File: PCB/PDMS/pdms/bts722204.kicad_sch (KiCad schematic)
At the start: 22 parts, among them IC7 BTS722204ESAXUMA1

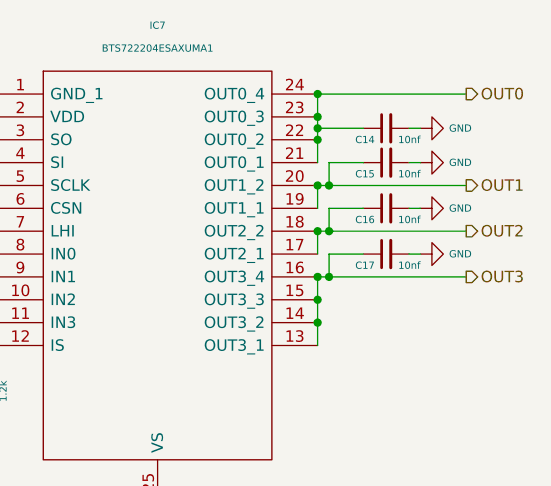
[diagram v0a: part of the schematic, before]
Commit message: Mostly assigned footprints
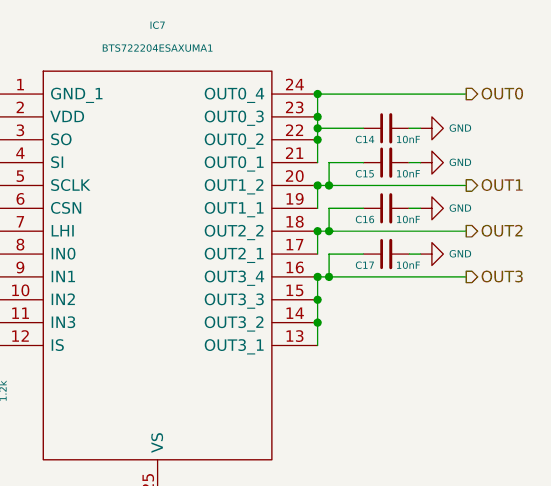
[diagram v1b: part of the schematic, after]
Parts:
- C14, C15, C16, C17: value 10nf -> 10nF
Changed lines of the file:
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@@
       (effects (font (size 0.8 0.8)) (justify left))
     )
-    (property "Value" "10nf" (id 1) (at 107.95 57.15 90)
+    (property "Value" "10nF" (id 1) (at 107.95 57.15 90)
       (effects (font (size 0.8 0.8)) (justify left))
     )
@@
       (effects (font (size 0.8 0.8)) (justify left))
     )
-    (property "Value" "10nf" (id 1) (at 107.95 48.26 90)
+    (property "Value" "10nF" (id 1) (at 107.95 48.26 90)
       (effects (font (size 0.8 0.8)) (justify left))
     )
@@
       (effects (font (size 0.8 0.8)) (justify left))
     )
-    (property "Value" "10nf" (id 1) (at 107.95 62.23 90)
+    (property "Value" "10nF" (id 1) (at 107.95 62.23 90)
       (effects (font (size 0.8 0.8)) (justify left))
     )
@@
       (effects (font (size 0.8 0.8)) (justify left))
     )
-    (property "Value" "10nf" (id 1) (at 107.95 52.07 90)
-      (effects (font (size 0.8 0.8)) (justify left))
-    )
+    (property "Value" "10nF" (id 1) (at 107.95 52.07 90)
+      (effects (font (size 0.8 0.8)) (justify left))
+    )

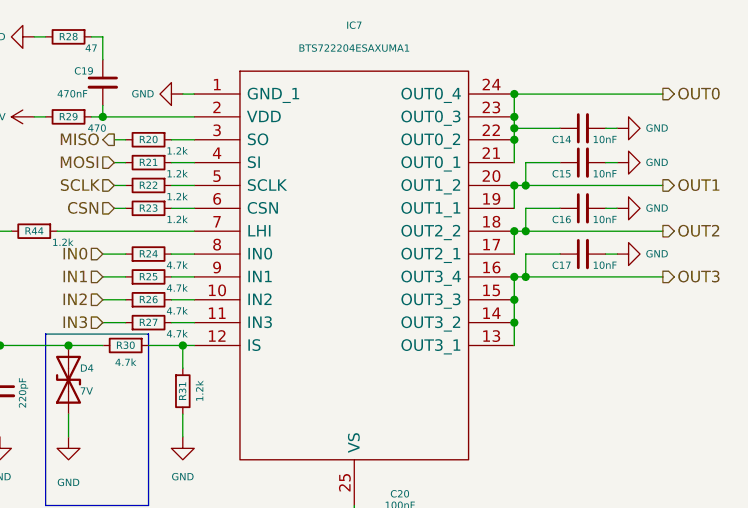
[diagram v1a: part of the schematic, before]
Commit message: Medium power stage layout
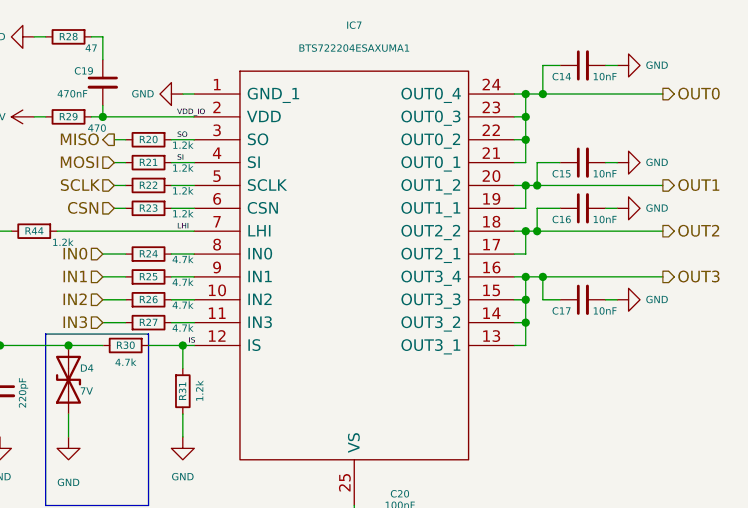
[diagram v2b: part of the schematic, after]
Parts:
- C14, C15, C16, C17: footprint Capacitor_SMD:C_0805_2012Metric -> Capacitor_SMD:C_0603_1608Metric
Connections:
- net LHI: now reaches IC7.7 (LHI), R44.1
- net VDD_IO: now reaches C19.2, IC7.2 (VDD), R29.1
- net IS: now reaches IC7.12 (IS), R30.1, R31.1
- net SO: now reaches IC7.3 (SO), R20.1
- net SI: now reaches IC7.4 (SI), R21.1
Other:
- moved on the sheet: C14, C17

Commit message: Imported 3.3V section with problematic shitty plugin
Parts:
- IC7: footprint PDM_Additional:SOP65P600X115-25N -> PDMS_Additional:SOP65P600X115-25N
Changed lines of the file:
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@@
       (effects (font (size 0.8 0.8)))
     )
-    (property "Footprint" "PDM_Additional:SOP65P600X115-25N" (id 2) (at 92.71 40.64 0)
+    (property "Footprint" "PDMS_Additional:SOP65P600X115-25N" (id 2) (at 92.71 40.64 0)
       (effects (font (size 1.27 1.27)) (justify left) hide)
     )

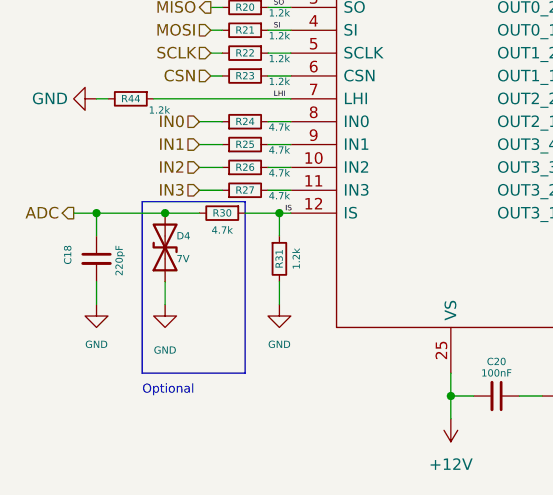
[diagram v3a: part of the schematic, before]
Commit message: Safety section - 74
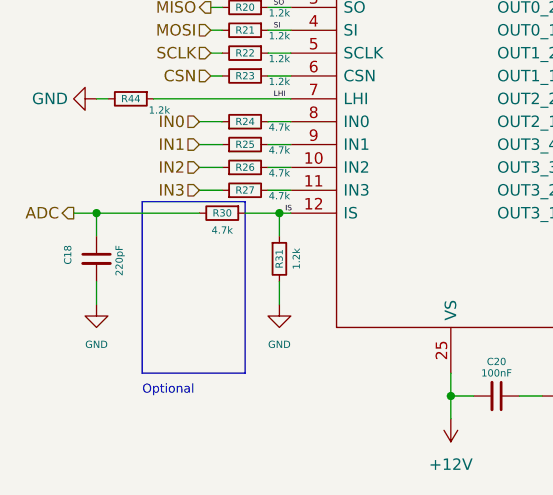
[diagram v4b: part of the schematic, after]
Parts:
- removed D4: 7V, Diode_SMD:D_0805_2012Metric, symbol Device:D_TVS
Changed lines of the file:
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@@
   (junction (at 97.79 58.42) (diameter 0) (color 0 0 0 0)
   )
-  (junction (at 46.99 71.12) (diameter 0) (color 0 0 0 0)
-  )
   (junction (at 97.79 68.58) (diameter 0) (color 0 0 0 0)
   )
@@
     (stroke (width 0) (type default) (color 0 0 0 0))
   )
-  (wire (pts (xy 39.37 71.12) (xy 46.99 71.12))
+  (wire (pts (xy 39.37 71.12) (xy 50.8 71.12))
     (stroke (width 0) (type default) (color 0 0 0 0))
   )
@@
     (stroke (width 0) (type default) (color 0 0 0 0))
   )
-  (wire (pts (xy 46.99 78.74) (xy 46.99 81.28))
-    (stroke (width 0) (type default) (color 0 0 0 0))
-  )
   (wire (pts (xy 58.42 53.34) (xy 60.96 53.34))
     (stroke (width 0) (type default) (color 0 0 0 0))
@@
   )
   (wire (pts (xy 101.6 55.88) (xy 99.06 55.88))
-    (stroke (width 0) (type default) (color 0 0 0 0))
-  )
-  (wire (pts (xy 46.99 71.12) (xy 50.8 71.12))
     (stroke (width 0) (type default) (color 0 0 0 0))
   )
@@
     (pin "9")
   )
-  (symbol (lib_id "power:GND") (at 46.99 81.28 0) (unit 1)
-    (in_bom yes) (on_board yes) (fields_autoplaced)
-    (property "Reference" "#PWR0134" (id 0) (at 46.99 87.63 0)
-      (effects (font (size 0.8 0.8)) hide)
-    )
-    (property "Value" "GND" (id 1) (at 46.99 86.36 0)
-      (effects (font (size 0.8 0.8)))
-    )
-    (property "Footprint" "" (id 2) (at 46.99 81.28 0)
-      (effects (font (size 1.27 1.27)) hide)
-    )
-    (property "Datasheet" "" (id 3) (at 46.99 81.28 0)
-      (effects (font (size 1.27 1.27)) hide)
-    )
-    (pin "1")
-  )
   (symbol (lib_id "power:GND") (at 107.95 66.04 90) (unit 1)
     (in_bom yes) (on_board yes) (fields_autoplaced)
@@
     (pin "1")
   )
-  (symbol (lib_id "Device:D_TVS") (at 46.99 74.93 90) (unit 1)
-    (in_bom yes) (on_board yes)
-    (property "Reference" "D4" (id 0) (at 48.26 73.66 90)
-      (effects (font (size 0.8 0.8)) (justify right))
-    )
-    (property "Value" "7V" (id 1) (at 48.26 76.2 90)
-      (effects (font (size 0.8 0.8)) (justify right))
-    )
-    (property "Footprint" "Diode_SMD:D_0805_2012Metric" (id 2) (at 46.99 74.93 0)
-      (effects (font (size 1.27 1.27)) hide)
-    )
-    (property "Datasheet" "~" (id 3) (at 46.99 74.93 0)
-      (effects (font (size 1.27 1.27)) hide)
-    )
-    (pin "1")
-    (pin "2")
-  )
   (symbol (lib_id "power:GND") (at 107.95 50.8 90) (unit 1)

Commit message: Major changes with new switch
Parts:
- added D39: BAT54SW, Package_TO_SOT_SMD:SOT-323_SC-70, symbol Diode:BAT54SW
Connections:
- net +3.3V: now also D39.2
- net ADC: now also D39.3
- net GND: now also D39.1
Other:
- note removed: "Optional"
- moved on the sheet: C18
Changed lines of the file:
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@@
   (junction (at 59.69 71.12) (diameter 0) (color 0 0 0 0)
   )
+  (junction (at 33.02 71.12) (diameter 0) (color 0 0 0 0)
+  )
   (junction (at 97.79 43.18) (diameter 0) (color 0 0 0 0)
   )
@@
   (junction (at 99.06 58.42) (diameter 0) (color 0 0 0 0)
   )
-  (junction (at 39.37 71.12) (diameter 0) (color 0 0 0 0)
+  (junction (at 45.974 71.12) (diameter 0) (color 0 0 0 0)
   )
   (junction (at 97.79 48.26) (diameter 0) (color 0 0 0 0)
@@
     (stroke (width 0) (type default) (color 0 0 0 0))
   )
-  (wire (pts (xy 39.37 71.12) (xy 50.8 71.12))
+  (wire (pts (xy 45.974 71.12) (xy 50.8 71.12))
     (stroke (width 0) (type default) (color 0 0 0 0))
   )
@@
     (stroke (width 0) (type default) (color 0 0 0 0))
   )
-  (polyline (pts (xy 44.45 69.85) (xy 44.45 88.9))
-    (stroke (width 0) (type default) (color 0 0 0 0))
-  )
   (wire (pts (xy 97.79 66.04) (xy 97.79 68.58))
     (stroke (width 0) (type default) (color 0 0 0 0))
@@
     (stroke (width 0) (type default) (color 0 0 0 0))
   )
-  (polyline (pts (xy 44.45 69.85) (xy 55.88 69.85))
-    (stroke (width 0) (type default) (color 0 0 0 0))
-  )
   (wire (pts (xy 50.8 66.04) (xy 53.34 66.04))
     (stroke (width 0) (type default) (color 0 0 0 0))
@@
     (stroke (width 0) (type default) (color 0 0 0 0))
   )
-  (wire (pts (xy 39.37 71.12) (xy 39.37 73.66))
+  (wire (pts (xy 45.974 71.12) (xy 45.974 73.66))
     (stroke (width 0) (type default) (color 0 0 0 0))
   )
@@
     (stroke (width 0) (type default) (color 0 0 0 0))
   )
+  (wire (pts (xy 41.275 80.772) (xy 40.64 80.772))
+    (stroke (width 0) (type default) (color 0 0 0 0))
+  )
   (wire (pts (xy 50.8 60.96) (xy 53.34 60.96))
     (stroke (width 0) (type default) (color 0 0 0 0))
@@
     (stroke (width 0) (type default) (color 0 0 0 0))
   )
-  (wire (pts (xy 36.83 71.12) (xy 39.37 71.12))
+  (wire (pts (xy 26.924 71.12) (xy 33.02 71.12))
     (stroke (width 0) (type default) (color 0 0 0 0))
   )
@@
     (stroke (width 0) (type default) (color 0 0 0 0))
   )
-  (wire (pts (xy 39.37 78.74) (xy 39.37 81.28))
+  (wire (pts (xy 45.974 78.74) (xy 45.974 80.772))
     (stroke (width 0) (type default) (color 0 0 0 0))
   )
@@
     (stroke (width 0) (type default) (color 0 0 0 0))
   )
-  (polyline (pts (xy 44.45 88.9) (xy 55.88 88.9))
-    (stroke (width 0) (type default) (color 0 0 0 0))
-  )
   (wire (pts (xy 55.88 71.12) (xy 59.69 71.12))
     (stroke (width 0) (type default) (color 0 0 0 0))
@@
     (stroke (width 0) (type default) (color 0 0 0 0))
   )
-  (polyline (pts (xy 55.88 88.9) (xy 55.88 69.85))
-    (stroke (width 0) (type default) (color 0 0 0 0))
-  )
   (wire (pts (xy 97.79 71.12) (xy 96.52 71.12))
     (stroke (width 0) (type default) (color 0 0 0 0))
   )
+  (wire (pts (xy 33.02 71.12) (xy 33.02 75.692))
+    (stroke (width 0) (type default) (color 0 0 0 0))
+  )
   (wire (pts (xy 97.79 48.26) (xy 97.79 45.72))
     (stroke (width 0) (type default) (color 0 0 0 0))
@@
     (stroke (width 0) (type default) (color 0 0 0 0))
   )
+  (wire (pts (xy 24.765 80.772) (xy 25.4 80.772))
+    (stroke (width 0) (type default) (color 0 0 0 0))
+  )
   (wire (pts (xy 59.69 78.74) (xy 59.69 81.28))
     (stroke (width 0) (type default) (color 0 0 0 0))
@@
     (stroke (width 0) (type default) (color 0 0 0 0))
   )
+  (wire (pts (xy 33.02 71.12) (xy 45.974 71.12))
+    (stroke (width 0) (type default) (color 0 0 0 0))
+  )
   (wire (pts (xy 78.74 91.44) (xy 81.28 91.44))
     (stroke (width 0) (type default) (color 0 0 0 0))
@@
   (wire (pts (xy 97.79 63.5) (xy 97.79 66.04))
     (stroke (width 0) (type default) (color 0 0 0 0))
-  )
-  (text "Optional" (at 44.45 91.44 0)
-    (effects (font (size 1 1)) (justify left bottom))
   )
   (label "IS" (at 60.325 71.12 0)
@@
     (effects (font (size 1.27 1.27)) (justify left))
   )
-  (hierarchical_label "ADC" (shape output) (at 36.83 71.12 180)
+  (hierarchical_label "ADC" (shape output) (at 26.924 71.12 180)
     (effects (font (size 1.27 1.27)) (justify right))
   )
   (hierarchical_label "IN3" (shape input) (at 50.8 68.58 180)
     (effects (font (size 1.27 1.27)) (justify right))
+  )
+  (symbol (lib_id "Diode:BAT54SW") (at 33.02 80.772 180) (unit 1)
+    (in_bom yes) (on_board yes) (fields_autoplaced)
+    (property "Reference" "D39" (id 0) (at 33.02 87.122 0))
+    (property "Value" "BAT54SW" (id 1) (at 33.02 84.582 0))
+    (property "Footprint" "Package_TO_SOT_SMD:SOT-323_SC-70" (id 2) (at 31.115 83.947 0)
+      (effects (font (size 1.27 1.27)) (justify left) hide)
+    )
+    (property "Datasheet" "https://assets.nexperia.com/documents/data-sheet/BAT54W_SER.pdf" (id 3) (at 36.068 80.772 0)
+      (effects (font (size 1.27 1.27)) hide)
+    )
+    (pin "1")
+    (pin "2")
+    (pin "3")
   )
   (symbol (lib_id "Device:R_Small") (at 55.88 68.58 90) (unit 1)
@@
     (pin "1")
   )
+  (symbol (lib_id "power:+3.3V") (at 24.765 80.772 90) (unit 1)
+    (in_bom yes) (on_board yes) (fields_autoplaced)
+    (property "Reference" "#PWR0417" (id 0) (at 28.575 80.772 0)
+      (effects (font (size 1.27 1.27)) hide)
+    )
+    (property "Value" "+3.3V" (id 1) (at 21.59 80.7721 90)
+      (effects (font (size 1.27 1.27)) (justify left))
+    )
+    (property "Footprint" "" (id 2) (at 24.765 80.772 0)
+      (effects (font (size 1.27 1.27)) hide)
+    )
+    (property "Datasheet" "" (id 3) (at 24.765 80.772 0)
+      (effects (font (size 1.27 1.27)) hide)
+    )
+    (pin "1")
+  )
   (symbol (lib_id "Device:R_Small") (at 59.69 76.2 0) (unit 1)
     (in_bom yes) (on_board yes)
@@
     (pin "2")
   )
-  (symbol (lib_id "Device:C_Small") (at 39.37 76.2 0) (unit 1)
-    (in_bom yes) (on_board yes)
-    (property "Reference" "C18" (id 0) (at 36.195 76.835 90)
-      (effects (font (size 0.8 0.8)) (justify left))
-    )
-    (property "Value" "220pF" (id 1) (at 41.91 78.105 90)
-      (effects (font (size 0.8 0.8)) (justify left))
-    )
-    (property "Footprint" "Capacitor_SMD:C_0402_1005Metric" (id 2) (at 39.37 76.2 0)
-      (effects (font (size 1.27 1.27)) hide)
-    )
-    (property "Datasheet" "~" (id 3) (at 39.37 76.2 0)
+  (symbol (lib_id "Device:C_Small") (at 45.974 76.2 0) (unit 1)
+    (in_bom yes) (on_board yes)
+    (property "Reference" "C18" (id 0) (at 42.799 76.835 90)
+      (effects (font (size 0.8 0.8)) (justify left))
+    )
+    (property "Value" "220pF" (id 1) (at 48.514 78.105 90)
+      (effects (font (size 0.8 0.8)) (justify left))
+    )
+    (property "Footprint" "Capacitor_SMD:C_0402_1005Metric" (id 2) (at 45.974 76.2 0)
+      (effects (font (size 1.27 1.27)) hide)
+    )
+    (property "Datasheet" "~" (id 3) (at 45.974 76.2 0)
       (effects (font (size 1.27 1.27)) hide)
     )
@@
     (pin "2")
   )
+  (symbol (lib_id "power:GND") (at 41.275 80.772 0) (unit 1)
+    (in_bom yes) (on_board yes) (fields_autoplaced)
+    (property "Reference" "#PWR0416" (id 0) (at 41.275 87.122 0)
+      (effects (font (size 1.27 1.27)) hide)
+    )
+    (property "Value" "GND" (id 1) (at 41.2751 83.947 90)
+      (effects (font (size 1.27 1.27)) (justify right))
+    )
+    (property "Footprint" "" (id 2) (at 41.275 80.772 0)
+      (effects (font (size 1.27 1.27)) hide)
+    )
+    (property "Datasheet" "" (id 3) (at 41.275 80.772 0)
+      (effects (font (size 1.27 1.27)) hide)
+    )
+    (pin "1")
+  )
   (symbol (lib_id "Device:R_Small") (at 55.88 55.88 270) (unit 1)
     (in_bom yes) (on_board yes)
@@
     (pin "1")
   )
-  (symbol (lib_id "power:GND") (at 39.37 81.28 0) (unit 1)
-    (in_bom yes) (on_board yes) (fields_autoplaced)
-    (property "Reference" "#PWR0131" (id 0) (at 39.37 87.63 0)
+  (symbol (lib_id "power:GND") (at 45.974 80.772 0) (unit 1)
+    (in_bom yes) (on_board yes) (fields_autoplaced)
+    (property "Reference" "#PWR0131" (id 0) (at 45.974 87.122 0)
       (effects (font (size 0.8 0.8)) hide)
     )
-    (property "Value" "GND" (id 1) (at 39.37 85.725 0)
-      (effects (font (size 0.8 0.8)))
-    )
-    (property "Footprint" "" (id 2) (at 39.37 81.28 0)
-      (effects (font (size 1.27 1.27)) hide)
-    )
-    (property "Datasheet" "" (id 3) (at 39.37 81.28 0)
-      (effects (font (size 1.27 1.27)) hide)
-    )
+    (property "Value" "GND" (id 1) (at 45.974 85.217 0)
+      (effects (font (size 0.8 0.8)))
+    )
+    (property "Footprint" "" (id 2) (at 45.974 80.772 0)
+      (effects (font (size 1.27 1.27)) hide)
+    )
+    (property "Datasheet" "" (id 3) (at 45.974 80.772 0)
+      (effects (font (size 1.27 1.27)) hide)
+    )

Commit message: PCB - Low power mosf voltage mux
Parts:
- C20: footprint Capacitor_SMD:C_0805_2012Metric -> Resistor_SMD:R_0402_1005Metric
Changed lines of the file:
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@@
       (effects (font (size 0.8 0.8)))
     )
-    (property "Footprint" "Capacitor_SMD:C_0805_2012Metric" (id 2) (at 83.82 91.44 0)
+    (property "Footprint" "Resistor_SMD:R_0402_1005Metric" (id 2) (at 83.82 91.44 0)
       (effects (font (size 1.27 1.27)) hide)
     )

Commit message: Finished 2024 version + gerbers
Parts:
- added D49: 3V3, Diode_SMD:D_SOD-523, symbol Device:D_Zener_Small
- added R114: 4.7k, Resistor_SMD:R_0402_1005Metric, symbol Device:R_Small
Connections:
- net ADC: no longer D39.3
- net GND: now also D49.2 (A)
- net IS: now also R114.2; no longer R30.1
- new net: D39.3, D49.1 (K), R114.1, R30.1
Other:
- note added: "Ris_prot -> value should be checked properly"
- note added: "SZMM5Z3V3T1G"
- moved on the sheet: C14, C15, C16, C17, C18, C19, C20, D39, IC7, R20, R21, R22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

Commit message: Clean-up of schematics
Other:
- note added: "BTS72220 - 4 channel high side switch"
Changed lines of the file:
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@@
     (effects (font (size 0.6 0.6)) (justify left bottom))
+  )
+  (text "BTS72220 - 4 channel high side switch" (at 187.198 191.135 0)
+    (effects (font (size 2 2) italic) (justify left bottom))
   )
   (text "SZMM5Z3V3T1G " (at 100.711 88.392 90)
